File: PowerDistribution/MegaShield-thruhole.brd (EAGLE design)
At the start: 109.2 x 53.3 mm, 40 parts, among them IC1 TLE5205-2, IC2 TLE5205-2, IC3 TLE5205-2, J10 DCJ0202

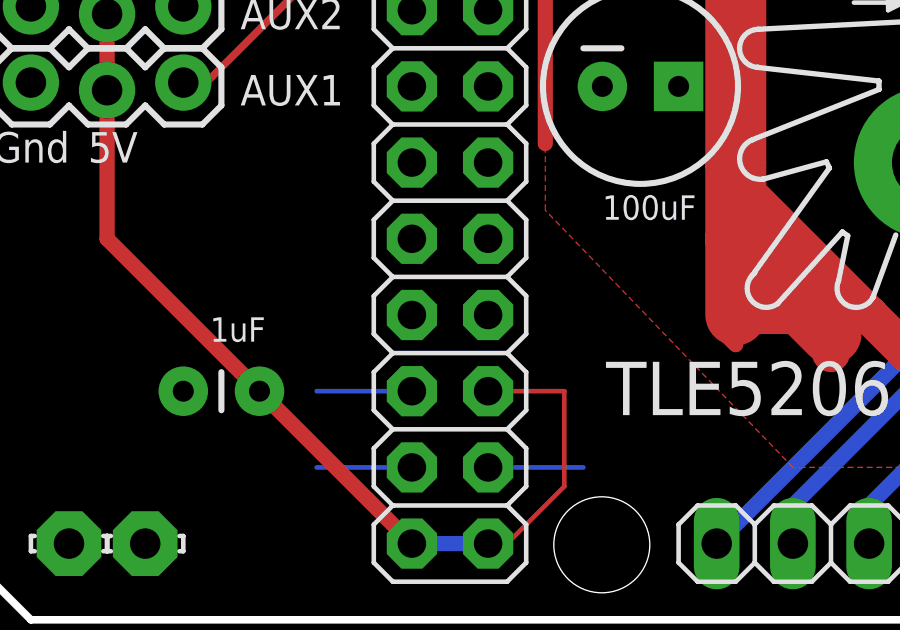
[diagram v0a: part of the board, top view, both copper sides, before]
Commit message: Move caps on schematic, change colors in SMD .brd
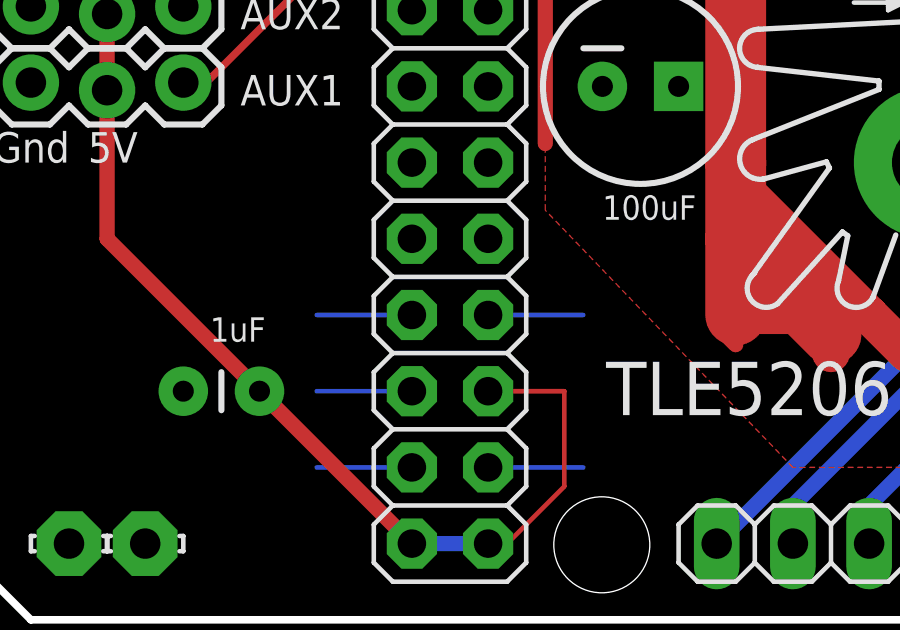
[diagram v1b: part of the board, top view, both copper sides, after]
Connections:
- removed net PA4: XIO.7
- removed net PA5: XIO.8
- net GND: now also XIO.7, XIO.8
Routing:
- net GND: track 35.8 -> 42.1 mm
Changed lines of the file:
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@@
 <contactref element="C7" pad="2"/>
 <contactref element="C8" pad="2"/>
+<contactref element="XIO" pad="7"/>
+<contactref element="XIO" pad="8"/>
+<wire x1="15.24" y1="10.16" x2="12.065" y2="10.16" width="0.1524" layer="16"/>
+<wire x1="17.78" y1="10.16" x2="20.955" y2="10.16" width="0.1524" layer="16"/>
 </signal>
 <signal name="INC2B">
@@
 <contactref element="XIO" pad="19"/>
 </signal>
-<signal name="PA4">
-<contactref element="XIO" pad="7"/>
-</signal>
-<signal name="PA5">
-<contactref element="XIO" pad="8"/>
-</signal>
 <signal name="PA6">
